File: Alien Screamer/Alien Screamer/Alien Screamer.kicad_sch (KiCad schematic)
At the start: 62 parts, among them J1 AudioJack2, J2 Conn_01x03, Q1 2N3904, Q2 2N3904, Q3 2N5457, U1 LM324, U2 LM386

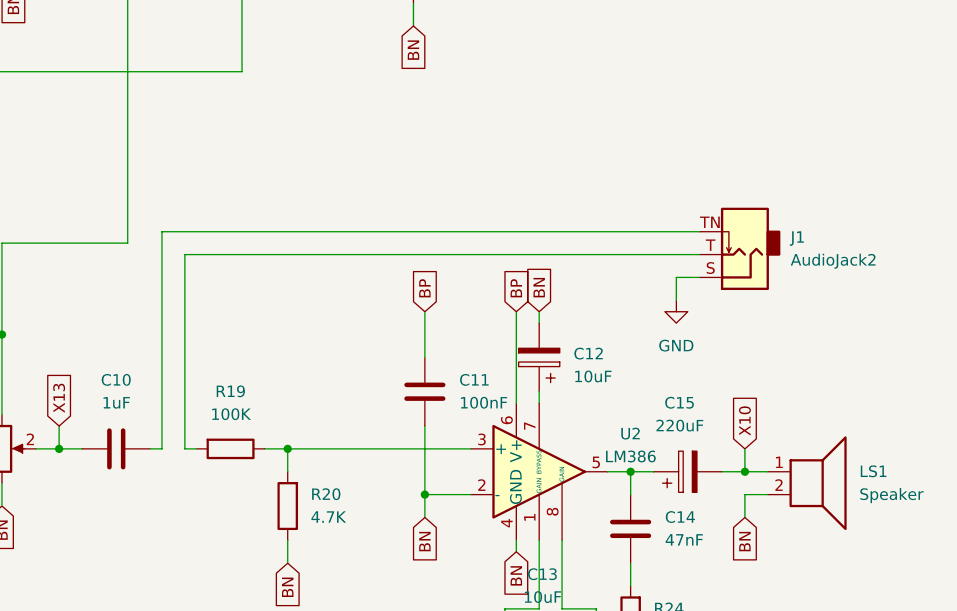
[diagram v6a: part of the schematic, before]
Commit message: Alien Screamer - fix audio jack
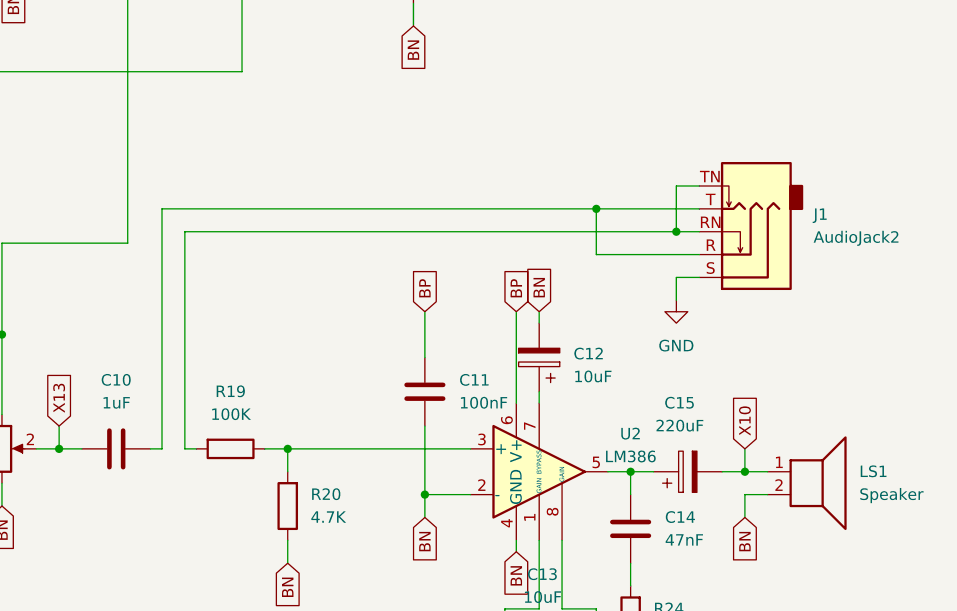
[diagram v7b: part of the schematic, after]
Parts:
- J1: symbol Connector-github:AudioJack2_SwitchT -> Connector-github:AudioJack3_SwitchTR
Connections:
- net at J1.T: now also C10.2, J1.R; no longer R19.2
- net at J1.TN: now also J1.RN, R19.2; no longer C10.2
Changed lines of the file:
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@@
   (junction (at 76.2 165.1) (diameter 0) (color 0 0 0 0)
   )
+  (junction (at 246.38 105.41) (diameter 0) (color 0 0 0 0)
+  )
   (junction (at 50.8 52.07) (diameter 0) (color 0 0 0 0)
   )
@@
   (junction (at 54.61 26.67) (diameter 0) (color 0 0 0 0)
   )
+  (junction (at 255.27 107.95) (diameter 0) (color 0 0 0 0)
+  )
   (junction (at 262.89 134.62) (diameter 0) (color 0 0 0 0)
   )
@@
     (stroke (width 0) (type default))
   )
-  (wire (pts (xy 198.12 132.08) (xy 198.12 107.95))
+  (wire (pts (xy 198.12 105.41) (xy 198.12 132.08))
     (stroke (width 0) (type default))
   )
@@
     (stroke (width 0) (type default))
   )
+  (wire (pts (xy 257.81 110.49) (xy 246.38 110.49))
+    (stroke (width 0) (type default))
+  )
   (wire (pts (xy 76.2 165.1) (xy 76.2 166.37))
     (stroke (width 0) (type default))
@@
     (stroke (width 0) (type default))
   )
+  (wire (pts (xy 257.81 105.41) (xy 246.38 105.41))
+    (stroke (width 0) (type default))
+  )
   (wire (pts (xy 88.9 165.1) (xy 76.2 165.1))
     (stroke (width 0) (type default))
@@
     (stroke (width 0) (type default))
   )
-  (wire (pts (xy 200.66 110.49) (xy 257.81 110.49))
-    (stroke (width 0) (type default))
-  )
   (wire (pts (xy 168.91 22.86) (xy 168.91 25.4))
     (stroke (width 0) (type default))
@@
     (stroke (width 0) (type default))
   )
-  (wire (pts (xy 200.66 132.08) (xy 200.66 110.49))
+  (wire (pts (xy 200.66 107.95) (xy 200.66 132.08))
     (stroke (width 0) (type default))
   )
@@
     (stroke (width 0) (type default))
   )
+  (wire (pts (xy 257.81 107.95) (xy 255.27 107.95))
+    (stroke (width 0) (type default))
+  )
   (wire (pts (xy 135.89 21.59) (xy 138.43 21.59))
     (stroke (width 0) (type default))
@@
     (stroke (width 0) (type default))
   )
-  (wire (pts (xy 198.12 107.95) (xy 257.81 107.95))
-    (stroke (width 0) (type default))
-  )
   (wire (pts (xy 265.43 137.16) (xy 262.89 137.16))
     (stroke (width 0) (type default))
@@
     (stroke (width 0) (type default))
   )
+  (wire (pts (xy 246.38 110.49) (xy 246.38 105.41))
+    (stroke (width 0) (type default))
+  )
   (wire (pts (xy 226.06 72.39) (xy 226.06 73.66))
     (stroke (width 0) (type default))
@@
     (stroke (width 0) (type default))
   )
+  (wire (pts (xy 246.38 105.41) (xy 198.12 105.41))
+    (stroke (width 0) (type default))
+  )
   (wire (pts (xy 72.39 40.64) (xy 68.58 40.64))
     (stroke (width 0) (type default))
@@
     (stroke (width 0) (type default))
   )
+  (wire (pts (xy 255.27 102.87) (xy 255.27 107.95))
+    (stroke (width 0) (type default))
+  )
   (wire (pts (xy 242.57 149.86) (xy 246.38 149.86))
     (stroke (width 0) (type default))
@@
     (stroke (width 0) (type default))
   )
+  (wire (pts (xy 255.27 107.95) (xy 200.66 107.95))
+    (stroke (width 0) (type default))
+  )
   (wire (pts (xy 17.78 157.48) (xy 22.86 157.48))
     (stroke (width 0) (type default))
@@
   )
   (wire (pts (xy 38.1 19.05) (xy 38.1 21.59))
+    (stroke (width 0) (type default))
+  )
+  (wire (pts (xy 257.81 102.87) (xy 255.27 102.87))
     (stroke (width 0) (type default))
   )
@@
     )
   )
-  (symbol (lib_id "Connector-github:AudioJack2_SwitchT") (at 262.89 110.49 180) (unit 1)
+  (symbol (lib_id "Connector-github:AudioJack3_SwitchTR") (at 262.89 110.49 180) (unit 1)
     (in_bom yes) (on_board yes) (dnp no) (fields_autoplaced)
-    (property "Reference" "J1" (at 267.97 108.585 0)
+    (property "Reference" "J1" (at 270.51 106.045 0)
       (effects (font (size 1.27 1.27)) (justify right))
     )
-    (property "Value" "AudioJack2" (at 267.97 111.125 0)
+    (property "Value" "AudioJack2" (at 270.51 108.585 0)
       (effects (font (size 1.27 1.27)) (justify right))
     )
@@
     (pin "T")
     (pin "TN")
+    (pin "R")
+    (pin "RN")
     (instances
       (project "Alien Screamer"

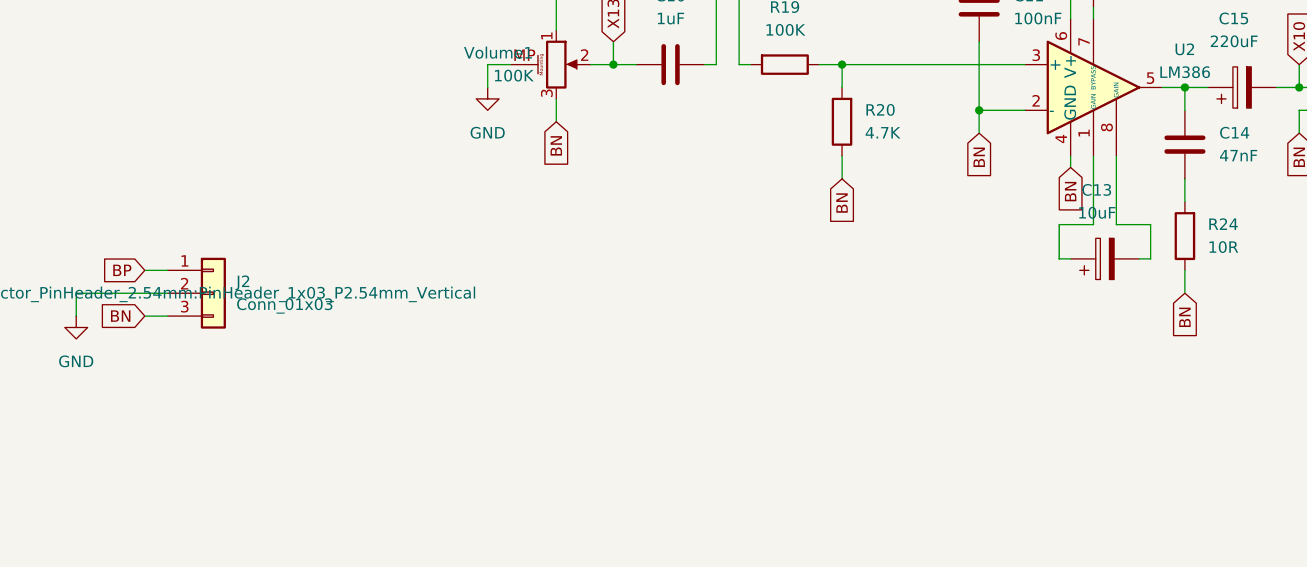
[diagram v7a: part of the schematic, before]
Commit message: Alien Screamer - fix switch orientation and remove optional components
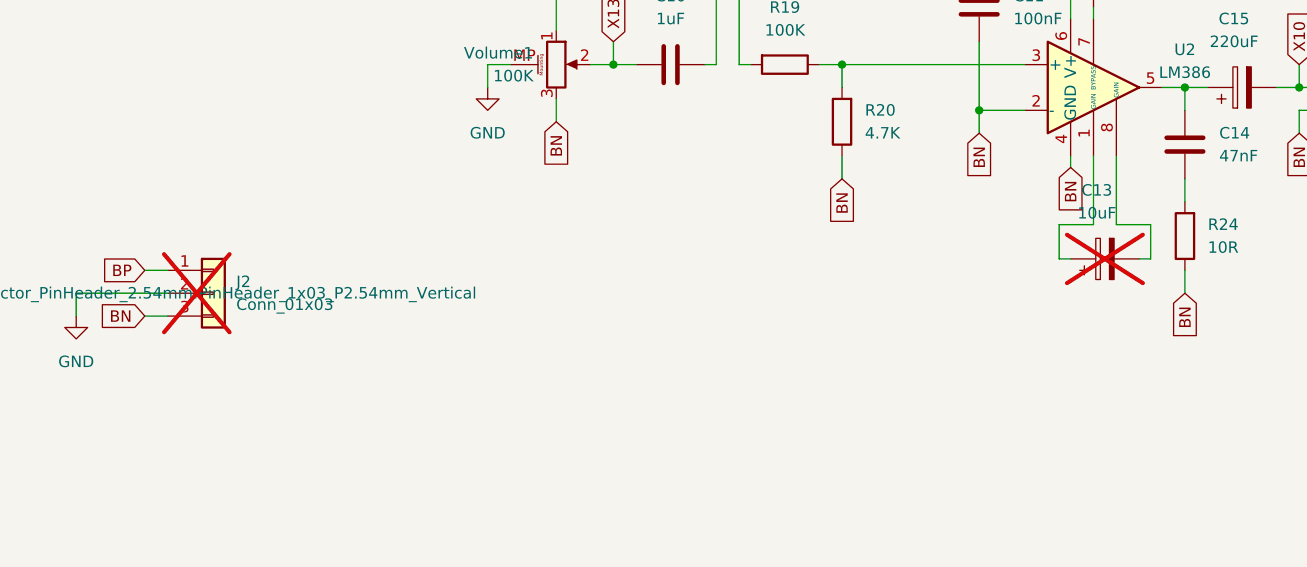
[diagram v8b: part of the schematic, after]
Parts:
- C13, J2: now not fitted; now left out of the parts list
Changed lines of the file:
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@@
   )
   (symbol (lib_id "Device:C_Polarized") (at 241.3 153.67 90) (unit 1)
-    (in_bom yes) (on_board yes) (dnp no) (fields_autoplaced)
+    (in_bom no) (on_board yes) (dnp yes) (fields_autoplaced)
     (property "Reference" "C13" (at 240.411 146.05 90)
       (effects (font (size 1.27 1.27)))
@@
   )
   (symbol (lib_id "Connector_Generic:Conn_01x03") (at 142.24 157.48 0) (unit 1)
-    (in_bom yes) (on_board yes) (dnp no) (fields_autoplaced)
+    (in_bom no) (on_board yes) (dnp yes) (fields_autoplaced)
     (property "Reference" "J2" (at 144.78 156.21 0)
       (effects (font (size 1.27 1.27)) (justify left))
